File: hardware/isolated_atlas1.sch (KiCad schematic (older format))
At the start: 15 parts, among them J301 CONN_01X02, P3 ATLAS_RTD_PROBE, U301 ADM3260, U302 ATLAS_RTD

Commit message: Trying out some test points.
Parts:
- added J11, J12: CONN_01x02, conservify:TP_Pads_D1.5mm_1x2, symbol conservify:CONN_01x02
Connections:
- wire segments 78 -> 82
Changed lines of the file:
@@
 NoConn ~ 3650 3000
 NoConn ~ 5200 3000
+Text Label 8350 4450 0    60   ~ 0
+ISO_GND
+Text Label 8350 4350 0    60   ~ 0
+ISO_VCC
+Text Label 8350 4100 0    60   ~ 0
+ISO_SCL
+Text Label 8350 4200 0    60   ~ 0
+ISO_SDA
+Wire Wire Line
+	8350 4100 8750 4100
+Wire Wire Line
+	8750 4200 8350 4200
+Wire Wire Line
+	8350 4350 8750 4350
+Wire Wire Line
+	8750 4450 8350 4450
+$Comp
+L conservify:CONN_01x02 J?
+U 1 1 5C0E925B
+P 8950 4100
+AR Path="/594C282A/5C0E925B" Ref="J?"  Part="1"
+AR Path="/594C3094/5C0E925B" Ref="J11"  Part="1"
+F 0 "J11" H 9029 4092 50  0000 L CNN
+F 1 "CONN_01x02" H 9029 4001 50  0000 L CNN
+F 2 "conservify:TP_Pads_D1.5mm_1x2" H 8950 4100 50  0001 C CNN
+F 3 "" H 8950 4100 50  0001 C CNN
+	1    8950 4100
+	1    0    0    -1
+$EndComp
+$Comp
+L conservify:CONN_01x02 J?
+U 1 1 5C0E9262
+P 8950 4350
+AR Path="/594C282A/5C0E9262" Ref="J?"  Part="1"
+AR Path="/594C3094/5C0E9262" Ref="J12"  Part="1"
+F 0 "J12" H 9029 4342 50  0000 L CNN
+F 1 "CONN_01x02" H 9029 4251 50  0000 L CNN
+F 2 "conservify:TP_Pads_D1.5mm_1x2" H 8950 4350 50  0001 C CNN
+F 3 "" H 8950 4350 50  0001 C CNN
+	1    8950 4350
+	1    0    0    -1
+$EndComp
 $EndSCHEMATC

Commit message: Add orientation indicator to SWD fp.
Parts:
- J11, J12: Critical (none) -> (none); MFN (none) -> (none); MFP (none) -> (none); Notes (none) -> (none); Package (none) -> (none); SPN1 (none) -> (none); Source (none) -> ANY; Subsystem (none) -> (none); Supplier1 (none) -> (none)
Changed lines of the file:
@@
+	1    0    0    -1
+$EndComp
+$Comp
+L conservify:CONN_01x02 J?
+U 1 1 5C0E925B
+P 8950 4100
+AR Path="/594C282A/5C0E925B" Ref="J?"  Part="1"
+AR Path="/594C3094/5C0E925B" Ref="J11"  Part="1"
+F 0 "J11" H 9029 4092 50  0000 L CNN
+F 1 "CONN_01x02" H 9029 4001 50  0000 L CNN
+F 2 "conservify:TP_Pads_D1.5mm_1x2" H 8950 4100 50  0001 C CNN
+F 3 "" H 8950 4100 50  0001 C CNN
+F 4 " " H 9029 4192 50  0001 C CNN "Critical"
+F 5 " " H 9029 4192 50  0001 C CNN "MFN"
+F 6 " " H 9029 4192 50  0001 C CNN "MFP"
+F 7 " " H 9029 4192 50  0001 C CNN "Notes"
+F 8 " " H 9029 4192 50  0001 C CNN "Package"
+F 9 " " H 9029 4192 50  0001 C CNN "SPN1"
+F 10 "ANY" H 9029 4192 50  0001 C CNN "Source"
+F 11 " " H 9029 4192 50  0001 C CNN "Subsystem"
+F 12 " " H 9029 4192 50  0001 C CNN "Supplier1"
+	1    8950 4100
+	1    0    0    -1
+$EndComp
+$Comp
+L conservify:CONN_01x02 J?
+U 1 1 5C0E9262
+P 8950 4350
+AR Path="/594C282A/5C0E9262" Ref="J?"  Part="1"
+AR Path="/594C3094/5C0E9262" Ref="J12"  Part="1"
+F 0 "J12" H 9029 4342 50  0000 L CNN
+F 1 "CONN_01x02" H 9029 4251 50  0000 L CNN
+F 2 "conservify:TP_Pads_D1.5mm_1x2" H 8950 4350 50  0001 C CNN
+F 3 "" H 8950 4350 50  0001 C CNN
+F 4 " " H 9029 4442 50  0001 C CNN "Critical"
+F 5 " " H 9029 4442 50  0001 C CNN "MFN"
+F 6 " " H 9029 4442 50  0001 C CNN "MFP"
+F 7 " " H 9029 4442 50  0001 C CNN "Notes"
+F 8 " " H 9029 4442 50  0001 C CNN "Package"
+F 9 " " H 9029 4442 50  0001 C CNN "SPN1"
+F 10 "ANY" H 9029 4442 50  0001 C CNN "Source"
+F 11 " " H 9029 4442 50  0001 C CNN "Subsystem"
+F 12 " " H 9029 4442 50  0001 C CNN "Supplier1"
+	1    8950 4350
 	1    0    0    -1
 $EndComp
@@
 Text Label 9450 2900 0    60   ~ 0
 RTD_PGND
+Text Label 8350 4450 0    60   ~ 0
+ISO_GND
+Text Label 8350 4350 0    60   ~ 0
+ISO_VCC
+Text Label 8350 4100 0    60   ~ 0
+ISO_SCL
+Text Label 8350 4200 0    60   ~ 0
+ISO_SDA
 Wire Wire Line
 	5200 3300 5350 3300
@@
 Wire Wire Line
 	6900 2500 7400 2500
+Wire Wire Line
+	8350 4100 8750 4100
+Wire Wire Line
+	8750 4200 8350 4200
+Wire Wire Line
+	8350 4350 8750 4350
+Wire Wire Line
+	8750 4450 8350 4450
 Connection ~ 5350 3500
 Connection ~ 5350 3400
@@
 NoConn ~ 3650 3000
 NoConn ~ 5200 3000
-Text Label 8350 4450 0    60   ~ 0
-ISO_GND
-Text Label 8350 4350 0    60   ~ 0
-ISO_VCC
-Text Label 8350 4100 0    60   ~ 0
-ISO_SCL
-Text Label 8350 4200 0    60   ~ 0
-ISO_SDA
-Wire Wire Line
-	8350 4100 8750 4100
-Wire Wire Line
-	8750 4200 8350 4200
-Wire Wire Line
-	8350 4350 8750 4350
-Wire Wire Line
-	8750 4450 8350 4450
-$Comp
-L conservify:CONN_01x02 J?
-U 1 1 5C0E925B
-P 8950 4100
-AR Path="/594C282A/5C0E925B" Ref="J?"  Part="1"
-AR Path="/594C3094/5C0E925B" Ref="J11"  Part="1"
-F 0 "J11" H 9029 4092 50  0000 L CNN
-F 1 "CONN_01x02" H 9029 4001 50  0000 L CNN
-F 2 "conservify:TP_Pads_D1.5mm_1x2" H 8950 4100 50  0001 C CNN
-F 3 "" H 8950 4100 50  0001 C CNN
-	1    8950 4100
-	1    0    0    -1
-$EndComp
-$Comp
-L conservify:CONN_01x02 J?
-U 1 1 5C0E9262
-P 8950 4350
-AR Path="/594C282A/5C0E9262" Ref="J?"  Part="1"
-AR Path="/594C3094/5C0E9262" Ref="J12"  Part="1"
-F 0 "J12" H 9029 4342 50  0000 L CNN
-F 1 "CONN_01x02" H 9029 4251 50  0000 L CNN
-F 2 "conservify:TP_Pads_D1.5mm_1x2" H 8950 4350 50  0001 C CNN
-F 3 "" H 8950 4350 50  0001 C CNN
-	1    8950 4350
-	1    0    0    -1
-$EndComp
 $EndSCHEMATC

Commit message: Started transition to 4 layer board
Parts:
- removed J11, J12: CONN_01x02, conservify:TP_Pads_D1.5mm_1x2, symbol conservify:CONN_01x02
- C301, C302, C303, C304, C305, C306: symbol conservify:CAPACITOR_CERAMIC -> fk-atlas-rescue:CAPACITOR_CERAMIC-conservify
- J301: symbol conservify:CONN_01x02 -> fk-atlas-rescue:CONN_01x02-conservify
- P3: symbol conservify:ATLAS_WATER_PROBE -> fk-atlas-rescue:ATLAS_WATER_PROBE-conservify
- R301, R302, R303, R304, R305: symbol conservify:R -> fk-atlas-rescue:R-conservify
- U301: symbol conservify:ADM3260 -> fk-atlas-rescue:ADM3260-conservify
- U302: footprint conservify:ATLAS_SENSOR_BOARD_RTD_OEM -> conservify:ATLAS_SENSOR_BOARD_RTD_COMBO; symbol conservify:ATLAS_SENSOR -> fk-atlas-rescue:ATLAS_SENSOR-conservify
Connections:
- wire segments 82 -> 78
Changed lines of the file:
@@
 $EndDescr
 $Comp
-L conservify:ADM3260 U301
+L fk-atlas-rescue:ADM3260-conservify U301
 U 1 1 594C2CF2
 P 4400 2900
@@
 $EndComp
 $Comp
-L conservify:CAPACITOR_CERAMIC C303
+L fk-atlas-rescue:CAPACITOR_CERAMIC-conservify C303
 U 1 1 594C2CF6
 P 5650 3800
@@
 $EndComp
 $Comp
-L conservify:CAPACITOR_CERAMIC C304
+L fk-atlas-rescue:CAPACITOR_CERAMIC-conservify C304
 U 1 1 594C2CF7
 P 5650 4100
@@
 $EndComp
 $Comp
-L conservify:CAPACITOR_CERAMIC C305
+L fk-atlas-rescue:CAPACITOR_CERAMIC-conservify C305
 U 1 1 5948D5A8
 P 5650 4400
@@
 $EndComp
 $Comp
-L conservify:CAPACITOR_CERAMIC C306
+L fk-atlas-rescue:CAPACITOR_CERAMIC-conservify C306
 U 1 1 594C2D02
 P 5650 4650
@@
 $EndComp
 $Comp
-L conservify:CAPACITOR_CERAMIC C301
+L fk-atlas-rescue:CAPACITOR_CERAMIC-conservify C301
 U 1 1 594C2D04
 P 2900 3800
@@
 $EndComp
 $Comp
-L conservify:CAPACITOR_CERAMIC C302
+L fk-atlas-rescue:CAPACITOR_CERAMIC-conservify C302
 U 1 1 594C2D09
 P 2900 4100
@@
 $EndComp
 $Comp
-L conservify:R R301
+L fk-atlas-rescue:R-conservify R301
 U 1 1 594C2D0C
 P 5650 3300
@@
 $EndComp
 $Comp
-L conservify:R R302
+L fk-atlas-rescue:R-conservify R302
 U 1 1 594C2D0F
 P 6250 2700
@@
 $EndComp
 $Comp
-L conservify:R R304
+L fk-atlas-rescue:R-conservify R304
 U 1 1 594C2D16
 P 6700 2700
@@
 $EndComp
 $Comp
-L conservify:R R303
+L fk-atlas-rescue:R-conservify R303
 U 1 1 594C2D1A
 P 6300 3250
@@
 $EndComp
 $Comp
-L conservify:R R305
+L fk-atlas-rescue:R-conservify R305
 U 1 1 5948E4EE
 P 6800 3250
@@
 $EndComp
 $Comp
-L conservify:VCC #PWR059
+L fk-atlas-rescue:VCC-conservify #PWR059
 U 1 1 594C2D23
 P 2450 3750
@@
 $EndComp
 $Comp
-L conservify:VCC #PWR060
+L fk-atlas-rescue:VCC-conservify #PWR060
 U 1 1 594C2D29
 P 2450 2350
@@
 $EndComp
 $Comp
-L conservify:ATLAS_SENSOR U302
+L fk-atlas-rescue:ATLAS_SENSOR-conservify U302
 U 1 1 594C2D36
 P 8550 2900
 F 0 "U302" H 8100 2550 60  0000 C CNN
 F 1 "ATLAS_RTD" H 8600 2850 60  0000 C CNN
-F 2 "conservify:ATLAS_SENSOR_BOARD_RTD_OEM" H 8550 2900 60  0001 C CNN
+F 2 "conservify:ATLAS_SENSOR_BOARD_RTD_COMBO" H 8550 2900 60  0001 C CNN
 F 3 "" H 8550 2900 60  0001 C CNN
 F 4 " " H 8100 2650 50  0001 C CNN "Critical"
@@
 $EndComp
 $Comp
-L conservify:CONN_01x02 J301
+L fk-atlas-rescue:CONN_01x02-conservify J301
 U 1 1 59A1BC7C
 P 10100 2900
@@
 $EndComp
 $Comp
-L conservify:ATLAS_WATER_PROBE P3
+L fk-atlas-rescue:ATLAS_WATER_PROBE-conservify P3
 U 1 1 59D29DF5
 P 8800 3550
@@
 $EndComp
 $Comp
-L conservify:PWR_FLAG #FLG0105
+L fk-atlas-rescue:PWR_FLAG-conservify #FLG0105
 U 1 1 5BCBBD88
 P 7400 4850
@@
 F 3 "~" H 7400 4850 50  0001 C CNN
 	1    7400 4850
-	1    0    0    -1
-$EndComp
-$Comp
-L conservify:CONN_01x02 J?
-U 1 1 5C0E925B
-P 8950 4100
-AR Path="/594C282A/5C0E925B" Ref="J?"  Part="1"
-AR Path="/594C3094/5C0E925B" Ref="J11"  Part="1"
-F 0 "J11" H 9029 4092 50  0000 L CNN
-F 1 "CONN_01x02" H 9029 4001 50  0000 L CNN
-F 2 "conservify:TP_Pads_D1.5mm_1x2" H 8950 4100 50  0001 C CNN
-F 3 "" H 8950 4100 50  0001 C CNN
-F 4 " " H 9029 4192 50  0001 C CNN "Critical"
-F 5 " " H 9029 4192 50  0001 C CNN "MFN"
-F 6 " " H 9029 4192 50  0001 C CNN "MFP"
-F 7 " " H 9029 4192 50  0001 C CNN "Notes"
-F 8 " " H 9029 4192 50  0001 C CNN "Package"
-F 9 " " H 9029 4192 50  0001 C CNN "SPN1"
-F 10 "ANY" H 9029 4192 50  0001 C CNN "Source"
-F 11 " " H 9029 4192 50  0001 C CNN "Subsystem"
-F 12 " " H 9029 4192 50  0001 C CNN "Supplier1"
-	1    8950 4100
-	1    0    0    -1
-$EndComp
-$Comp
-L conservify:CONN_01x02 J?
-U 1 1 5C0E9262
-P 8950 4350
-AR Path="/594C282A/5C0E9262" Ref="J?"  Part="1"
-AR Path="/594C3094/5C0E9262" Ref="J12"  Part="1"
-F 0 "J12" H 9029 4342 50  0000 L CNN
-F 1 "CONN_01x02" H 9029 4251 50  0000 L CNN
-F 2 "conservify:TP_Pads_D1.5mm_1x2" H 8950 4350 50  0001 C CNN
-F 3 "" H 8950 4350 50  0001 C CNN
-F 4 " " H 9029 4442 50  0001 C CNN "Critical"
-F 5 " " H 9029 4442 50  0001 C CNN "MFN"
-F 6 " " H 9029 4442 50  0001 C CNN "MFP"
-F 7 " " H 9029 4442 50  0001 C CNN "Notes"
-F 8 " " H 9029 4442 50  0001 C CNN "Package"
-F 9 " " H 9029 4442 50  0001 C CNN "SPN1"
-F 10 "ANY" H 9029 4442 50  0001 C CNN "Source"
-F 11 " " H 9029 4442 50  0001 C CNN "Subsystem"
-F 12 " " H 9029 4442 50  0001 C CNN "Supplier1"
-	1    8950 4350
 	1    0    0    -1
 $EndComp
@@
 Text Label 9450 2900 0    60   ~ 0
 RTD_PGND
-Text Label 8350 4450 0    60   ~ 0
-ISO_GND
-Text Label 8350 4350 0    60   ~ 0
-ISO_VCC
-Text Label 8350 4100 0    60   ~ 0
-ISO_SCL
-Text Label 8350 4200 0    60   ~ 0
-ISO_SDA
 Wire Wire Line
 	5200 3300 5350 3300
@@
 Wire Wire Line
 	6900 2500 7400 2500
-Wire Wire Line
-	8350 4100 8750 4100
-Wire Wire Line
-	8750 4200 8350 4200
-Wire Wire Line
-	8350 4350 8750 4350
-Wire Wire Line
-	8750 4450 8350 4450
 Connection ~ 5350 3500
 Connection ~ 5350 3400

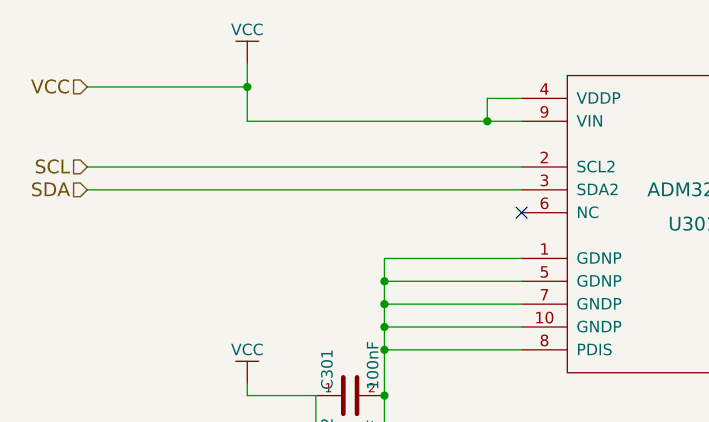
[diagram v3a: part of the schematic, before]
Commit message: Added pull up resistors and a debounce cap for the reset button
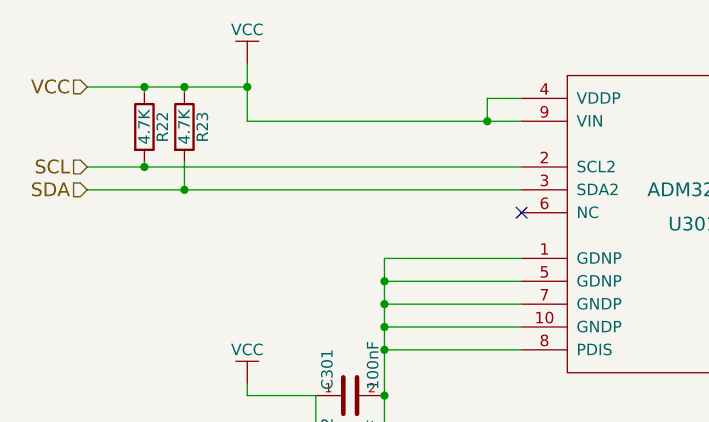
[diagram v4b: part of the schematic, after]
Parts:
- added R22, R23: 4.7K, conservify:RES-0603, symbol fk-atlas-rescue:R-conservify
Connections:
- net SCL: now also R22.2
- net SDA: now also R23.2
- net VCC: now also R22.1, R23.1
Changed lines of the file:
@@
 	2450 3800 2450 3750
 Wire Wire Line
-	1750 2800 3650 2800
+	1750 2800 2000 2800
 Wire Wire Line
-	1750 2900 3650 2900
+	1750 2900 2175 2900
 Wire Wire Line
-	1750 2450 2450 2450
+	1750 2450 2000 2450
 Wire Wire Line
 	5350 5000 7400 5000
@@
 NoConn ~ 3650 3000
 NoConn ~ 5200 3000
+$Comp
+L fk-atlas-rescue:R-conservify R22
+U 1 1 5C7F5CBD
+P 2000 2625
+F 0 "R22" V 2080 2625 50  0000 C CNN
+F 1 "4.7K" V 2000 2625 50  0000 C CNN
+F 2 "conservify:RES-0603" V 1930 2625 50  0001 C CNN
+F 3 "" H 2000 2625 50  0001 C CNN
+F 4 " " H 2080 2725 50  0001 C CNN "Critical"
+F 5 "Yageo" H 2080 2725 50  0001 C CNN "MFN"
+F 6 "AF0603JR-074K7L" H 2080 2725 50  0001 C CNN "MFP"
+F 7 " " H 2080 2725 50  0001 C CNN "Notes"
+F 8 " " H 2080 2725 50  0001 C CNN "Package"
+F 9 "ANY" H 2080 2725 50  0001 C CNN "Source"
+F 10 " " H 2080 2725 50  0001 C CNN "Subsystem"
+F 11 "mouser" H 2080 2725 50  0001 C CNN "Supplier1"
+F 12 "0" H 2080 2725 50  0001 C CNN "price"
+F 13 "603-AF0603JR-074K7L" H -4300 -625 50  0001 C CNN "spn1"
+F 14 "mouser" H -4300 -625 50  0001 C CNN "spn2"
+	1    2000 2625
+	1    0    0    -1
+$EndComp
+Wire Wire Line
+	2000 2475 2000 2450
+Connection ~ 2000 2450
+Wire Wire Line
+	2000 2450 2175 2450
+Wire Wire Line
+	2000 2775 2000 2800
+Connection ~ 2000 2800
+Wire Wire Line
+	2000 2800 3650 2800
+$Comp
+L fk-atlas-rescue:R-conservify R23
+U 1 1 5C7F97D8
+P 2175 2625
+F 0 "R23" V 2255 2625 50  0000 C CNN
+F 1 "4.7K" V 2175 2625 50  0000 C CNN
+F 2 "conservify:RES-0603" V 2105 2625 50  0001 C CNN
+F 3 "" H 2175 2625 50  0001 C CNN
+F 4 " " H 2255 2725 50  0001 C CNN "Critical"
+F 5 "Yageo" H 2255 2725 50  0001 C CNN "MFN"
+F 6 "AF0603JR-074K7L" H 2255 2725 50  0001 C CNN "MFP"
+F 7 " " H 2255 2725 50  0001 C CNN "Notes"
+F 8 " " H 2255 2725 50  0001 C CNN "Package"
+F 9 "ANY" H 2255 2725 50  0001 C CNN "Source"
+F 10 " " H 2255 2725 50  0001 C CNN "Subsystem"
+F 11 "mouser" H 2255 2725 50  0001 C CNN "Supplier1"
+F 12 "0" H 2255 2725 50  0001 C CNN "price"
+F 13 "603-AF0603JR-074K7L" H -4125 -625 50  0001 C CNN "spn1"
+F 14 "mouser" H -4125 -625 50  0001 C CNN "spn2"
+	1    2175 2625
+	1    0    0    -1
+$EndComp
+Wire Wire Line
+	2175 2475 2175 2450
+Connection ~ 2175 2450
+Wire Wire Line
+	2175 2450 2450 2450
+Wire Wire Line
+	2175 2775 2175 2900
+Connection ~ 2175 2900
+Wire Wire Line
+	2175 2900 3650 2900
 $EndSCHEMATC
